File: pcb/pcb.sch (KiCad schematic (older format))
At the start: 116 parts, among them J1 USB_C_Receptacle_USB2.0, SW1 SW_Push, SW10 SW_Push, SW11 SW_Push, SW12 SW_Push, SW13 SW_Push, SW14 SW_Push, SW15 SW_Push, SW16 SW_Push, SW17 SW_Push, SW18 SW_Push, SW19 SW_Push, SW2 SW_Push, SW20 SW_Push, SW21 SW_Push, SW22 SW_Push, SW23 SW_Push, SW24 SW_Push, SW25 SW_Push, SW26 SW_Push, SW27 SW_Push, SW28 SW_Push, SW29 SW_Push, SW3 SW_Push, SW30 SW_Push, SW31 SW_Push, SW32 SW_Push, SW33 SW_Push, SW34 SW_Push, SW35 SW_Push, SW36 SW_Push, SW37 SW_Push, SW38 SW_Push, SW39 SW_Push, SW4 SW_Push, SW40 SW_Push, SW41 SW_Push, SW42 SW_Push, SW43 SW_Push, SW44 SW_Push, SW45 SW_Push, SW46 SW_Push, SW47 SW_Push, SW48 SW_Push, SW49 SW_Push, SW5 SW_Push, SW6 SW_Push, SW7 SW_Push, SW8 SW_Push, SW9 SW_Push, U1 ATmega32U4-AU, Y1 16MHz

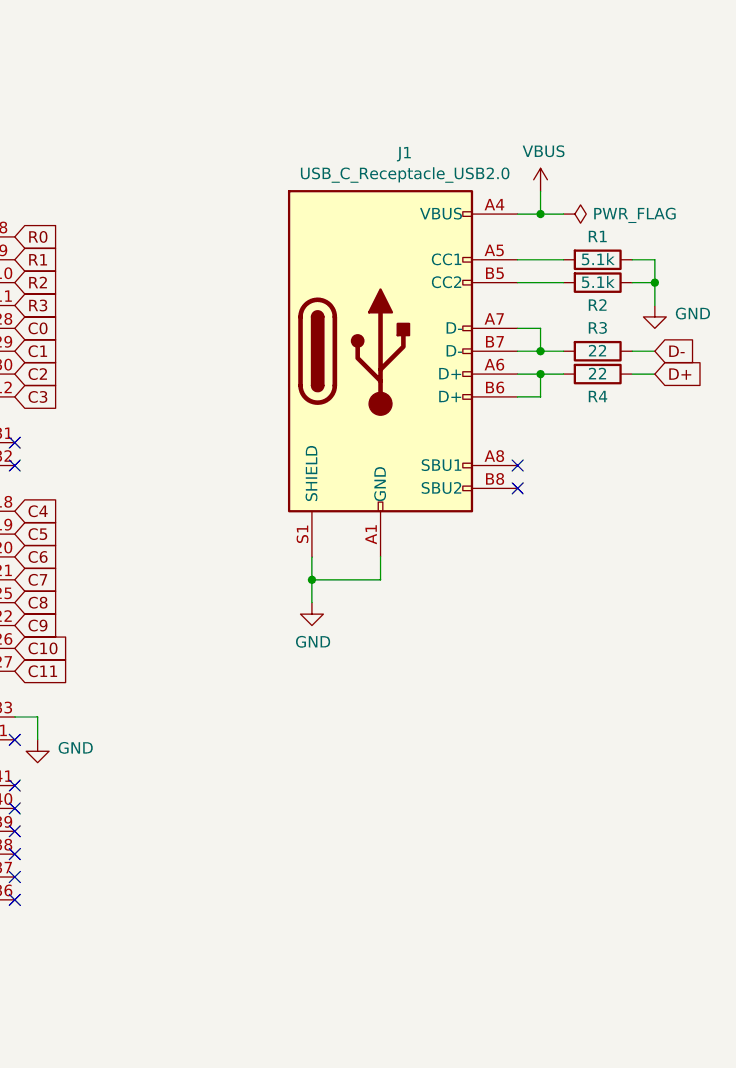
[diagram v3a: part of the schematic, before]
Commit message: update USB-C pins
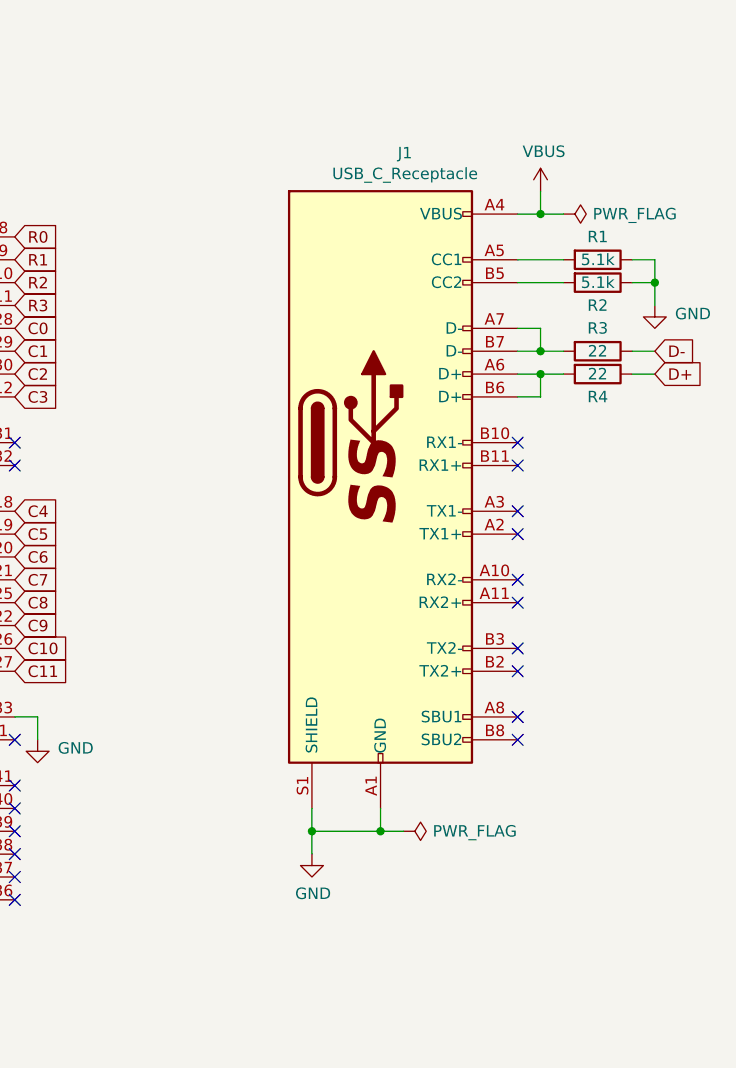
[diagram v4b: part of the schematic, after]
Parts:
- removed J1: USB_C_Receptacle_USB2.0, digikey-footprints:USB-C_Female_CX70M-24P1, symbol Connector:USB_C_Receptacle_USB2.0
- added J1: USB_C_Receptacle, digikey-footprints:USB-C_Female_CX70M-24P1, symbol Connector:USB_C_Receptacle
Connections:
- net GND: now also J1.A1 (GND), J1.A12 (GND), J1.B1 (GND), J1.B12 (GND), J1.S1 (SHIELD)
- net VBUS: now also J1.A4 (VBUS), J1.A9 (VBUS), J1.B4 (VBUS), J1.B9 (VBUS)
- net at R1.2: now also J1.A5 (CC1)
- net at R4.2: now also J1.A6 (D+), J1.B6 (D+)
- net at R3.2: now also J1.A7 (D-), J1.B7 (D-)
- net at R2.2: now also J1.B5 (CC2)
- no-connect marks 11 -> 19
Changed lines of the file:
@@
 	6350 5700 6350 5800
-$Comp
-L Connector:USB_C_Receptacle_USB2.0 J1
-U 1 1 5D13142D
-P 7850 4100
-F 0 "J1" H 7957 4967 50  0000 C CNN
-F 1 "USB_C_Receptacle_USB2.0" H 7957 4876 50  0000 C CNN
-F 2 "digikey-footprints:USB-C_Female_CX70M-24P1" H 8000 4100 50  0001 C CNN
-F 3 "https://www.usb.org/sites/default/files/documents/usb_type-c.zip" H 8000 4100 50  0001 C CNN
-	1    7850 4100
-	1    0    0    -1
-$EndComp
 $Comp
 L power:GND #PWR010
 U 1 1 5D1342DD
-P 7550 5200
-F 0 "#PWR010" H 7550 4950 50  0001 C CNN
-F 1 "GND" H 7555 5027 50  0000 C CNN
-F 2 "" H 7550 5200 50  0001 C CNN
-F 3 "" H 7550 5200 50  0001 C CNN
-	1    7550 5200
-	1    0    0    -1
-$EndComp
-Wire Wire Line
-	7550 5000 7550 5100
-Wire Wire Line
-	7550 5100 7850 5100
-Wire Wire Line
-	7850 5100 7850 5000
-Connection ~ 7550 5100
-Wire Wire Line
-	7550 5100 7550 5200
+P 7550 6300
+F 0 "#PWR010" H 7550 6050 50  0001 C CNN
+F 1 "GND" H 7555 6127 50  0000 C CNN
+F 2 "" H 7550 6300 50  0001 C CNN
+F 3 "" H 7550 6300 50  0001 C CNN
+	1    7550 6300
+	1    0    0    -1
+$EndComp
+Wire Wire Line
+	7550 6100 7550 6200
+Wire Wire Line
+	7550 6200 7850 6200
+Wire Wire Line
+	7850 6200 7850 6100
+Connection ~ 7550 6200
+Wire Wire Line
+	7550 6200 7550 6300
 NoConn ~ 8450 4600
-NoConn ~ 8450 4700
+NoConn ~ 8450 4500
 $Comp
 L power:VBUS #PWR02
@@
 	1    0    0    -1
 $EndComp
+$Comp
+L Connector:USB_C_Receptacle J1
+U 1 1 5D16305C
+P 7850 4500
+F 0 "J1" H 7957 5767 50  0000 C CNN
+F 1 "USB_C_Receptacle" H 7957 5676 50  0000 C CNN
+F 2 "digikey-footprints:USB-C_Female_CX70M-24P1" H 8000 4500 50  0001 C CNN
+F 3 "https://www.usb.org/sites/default/files/documents/usb_type-c.zip" H 8000 4500 50  0001 C CNN
+	1    7850 4500
+	1    0    0    -1
+$EndComp
+NoConn ~ 8450 4800
+NoConn ~ 8450 4900
+NoConn ~ 8450 5100
+NoConn ~ 8450 5200
+NoConn ~ 8450 5400
+NoConn ~ 8450 5500
+NoConn ~ 8450 5700
+NoConn ~ 8450 5800
+$Comp
+L power:PWR_FLAG #FLG02
+U 1 1 5D307145
+P 7950 6200
+F 0 "#FLG02" H 7950 6275 50  0001 C CNN
+F 1 "PWR_FLAG" V 7950 6328 50  0000 L CNN
+F 2 "" H 7950 6200 50  0001 C CNN
+F 3 "~" H 7950 6200 50  0001 C CNN
+	1    7950 6200
+	0    1    1    0
+$EndComp
+Wire Wire Line
+	7850 6200 7950 6200
+Connection ~ 7850 6200
 $EndSCHEMATC

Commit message: add PCB & gerber
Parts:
- removed C3: 0.1u, Capacitor_SMD:C_1206_3216Metric_Pad1.42x1.75mm_HandSolder, symbol Device:C
- removed R6, R7: 22, Resistor_SMD:R_1206_3216Metric_Pad1.42x1.75mm_HandSolder, symbol Device:R
- removed SW49: SW_Push, Button_Switch_THT:SW_PUSH_6mm_H5mm, symbol Switch:SW_Push
- added H1, H2, H3, H4, H5, H6, H7, H8: MountingHole, MountingHole:MountingHole_3.5mm, symbol Mechanical:MountingHole
- added JP1: SolderJumper_2_Open, Jumper:SolderJumper-2_P1.3mm_Open_Pad1.0x1.5mm, symbol Jumper:SolderJumper_2_Open
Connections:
- net VBUS is gone; now on net VCC: J1.A4 (VBUS), J1.A9 (VBUS), J1.B4 (VBUS), J1.B9 (VBUS), U1.7 (VBUS)
- net C0: now also U1.22 (PD5); no longer U1.28 (PB4)
- net C1: now also U1.21 (PD3); no longer U1.29 (PB5)
- net C11: now also U1.25 (PD4); no longer U1.27 (PD7)
- net C2: now also U1.20 (PD2); no longer U1.30 (PB6)
- net C3: now also U1.19 (PD1); no longer U1.12 (PB7)
- net C5: now also U1.12 (PB7); no longer U1.19 (PD1)
- net C6: now also U1.30 (PB6); no longer U1.20 (PD2)
- net C7: now also U1.29 (PB5); no longer U1.21 (PD3)
- net C8: now also U1.28 (PB4); no longer U1.25 (PD4)
- net C9: now also U1.27 (PD7); no longer U1.22 (PD5)
- net D+: now also U1.4 (D+)
- net D-: now also U1.3 (D-)
- net GND: now also JP1.2 (B)
- net RESET: now also JP1.1 (A)
- no-connect marks 19 -> 20
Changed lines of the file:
@@
 	1    0    0    -1
 $EndComp
-$Comp
-L Device:R R6
-U 1 1 5D0E382B
-P 4850 4600
-F 0 "R6" V 4750 4600 50  0000 C CNN
-F 1 "22" V 4850 4600 50  0000 C CNN
-F 2 "Resistor_SMD:R_1206_3216Metric_Pad1.42x1.75mm_HandSolder" H 4850 4600 50  0001 C CNN
-F 3 "~" H 4850 4600 50  0001 C CNN
-	1    4850 4600
-	0    1    1    0
-$EndComp
-Wire Wire Line
-	5000 4600 5050 4600
-Wire Wire Line
-	5000 4700 5050 4700
-Text GLabel 4650 4600 0    50   Input ~ 0
+Wire Wire Line
+	4950 4600 5050 4600
+Wire Wire Line
+	4950 4700 5050 4700
+Text GLabel 4950 4600 0    50   Input ~ 0
 D+
-Text GLabel 4650 4700 0    50   Input ~ 0
+Text GLabel 4950 4700 0    50   Input ~ 0
 D-
-Wire Wire Line
-	4650 4600 4700 4600
-Wire Wire Line
-	4650 4700 4700 4700
-$Comp
-L Device:R R7
-U 1 1 5D0E023D
-P 4850 4700
-F 0 "R7" V 4950 4700 50  0000 C CNN
-F 1 "22" V 4850 4700 50  0000 C CNN
-F 2 "Resistor_SMD:R_1206_3216Metric_Pad1.42x1.75mm_HandSolder" H 4850 4700 50  0001 C CNN
-F 3 "~" H 4850 4700 50  0001 C CNN
-	1    4850 4700
-	0    1    1    0
-$EndComp
 Wire Wire Line
 	2800 2400 2900 2400
@@
 	1    0    0    -1
 $EndComp
-Wire Wire Line
-	4400 4200 5050 4200
-Wire Wire Line
-	5050 4400 4600 4400
-Wire Wire Line
-	4600 4400 4600 4100
-$Comp
-L power:VBUS #PWR06
-U 1 1 5DD88E79
-P 4600 4100
-F 0 "#PWR06" H 4600 3950 50  0001 C CNN
-F 1 "VBUS" H 4543 4137 50  0000 R CNN
-F 2 "" H 4600 4100 50  0001 C CNN
-F 3 "" H 4600 4100 50  0001 C CNN
-	1    4600 4100
-	1    0    0    -1
-$EndComp
-$Comp
-L power:GND #PWR08
-U 1 1 5DD48EDC
-P 4400 4700
-F 0 "#PWR08" H 4400 4450 50  0001 C CNN
-F 1 "GND" H 4322 4663 50  0000 R CNN
-F 2 "" H 4400 4700 50  0001 C CNN
-F 3 "" H 4400 4700 50  0001 C CNN
-	1    4400 4700
-	1    0    0    -1
-$EndComp
-$Comp
-L Device:C C3
-U 1 1 5DD8B658
-P 4400 4450
-F 0 "C3" H 4285 4496 50  0000 R CNN
-F 1 "0.1u" H 4285 4405 50  0000 R CNN
-F 2 "Capacitor_SMD:C_1206_3216Metric_Pad1.42x1.75mm_HandSolder" H 4438 4300 50  0001 C CNN
-F 3 "~" H 4400 4450 50  0001 C CNN
-	1    4400 4450
-	1    0    0    -1
-$EndComp
-Wire Wire Line
-	4400 4300 4400 4200
-Wire Wire Line
-	4400 4700 4400 4600
 $Comp
 L Device:C C4
@@
 Text GLabel 6250 3900 2    50   Input ~ 0
 R3
-Text GLabel 6250 4000 2    50   Input ~ 0
+Text GLabel 6250 5300 2    50   Input ~ 0
 C0
-Text GLabel 6250 4100 2    50   Input ~ 0
+Text GLabel 6250 5100 2    50   Input ~ 0
 C1
-Text GLabel 6250 4200 2    50   Input ~ 0
+Text GLabel 6250 5000 2    50   Input ~ 0
 C2
-Text GLabel 6250 4300 2    50   Input ~ 0
+Text GLabel 6250 4900 2    50   Input ~ 0
 C3
 Text GLabel 6250 4800 2    50   Input ~ 0
 C4
-Text GLabel 6250 4900 2    50   Input ~ 0
+Text GLabel 6250 4300 2    50   Input ~ 0
 C5
-Text GLabel 6250 5000 2    50   Input ~ 0
+Text GLabel 6250 4200 2    50   Input ~ 0
 C6
-Text GLabel 6250 5100 2    50   Input ~ 0
+Text GLabel 6250 4100 2    50   Input ~ 0
 C7
-Text GLabel 6250 5200 2    50   Input ~ 0
+Text GLabel 6250 4000 2    50   Input ~ 0
 C8
-Text GLabel 6250 5300 2    50   Input ~ 0
+Text GLabel 6250 5500 2    50   Input ~ 0
 C9
 Text GLabel 6250 5400 2    50   Input ~ 0
 C10
-Text GLabel 6250 5500 2    50   Input ~ 0
+Text GLabel 6250 5200 2    50   Input ~ 0
 C11
 NoConn ~ 6250 4500
@@
 NoConn ~ 8450 4600
 NoConn ~ 8450 4500
-$Comp
-L power:VBUS #PWR02
-U 1 1 5D10FDDC
-P 8550 3400
-F 0 "#PWR02" H 8550 3250 50  0001 C CNN
-F 1 "VBUS" H 8565 3573 50  0000 C CNN
-F 2 "" H 8550 3400 50  0001 C CNN
-F 3 "" H 8550 3400 50  0001 C CNN
-	1    8550 3400
-	1    0    0    -1
-$EndComp
 Wire Wire Line
 	8450 3500 8550 3500
 Wire Wire Line
 	8550 3500 8550 3400
-Wire Wire Line
-	8650 3500 8550 3500
-Connection ~ 8550 3500
-$Comp
-L power:PWR_FLAG #FLG01
-U 1 1 5D148DCF
-P 8650 3500
-F 0 "#FLG01" H 8650 3575 50  0001 C CNN
-F 1 "PWR_FLAG" V 8650 3628 50  0000 L CNN
-F 2 "" H 8650 3500 50  0001 C CNN
-F 3 "~" H 8650 3500 50  0001 C CNN
-	1    8650 3500
-	0    1    1    0
-$EndComp
 $Comp
 L Device:R R1
@@
 	1    0    0    -1
 $EndComp
-$Comp
-L Switch:SW_Push SW49
-U 1 1 5D439BB1
-P 3050 4700
-F 0 "SW49" H 3150 4800 50  0000 C CNN
-F 1 "SW_Push" H 3050 4650 50  0000 C CNN
-F 2 "Button_Switch_THT:SW_PUSH_6mm_H5mm" H 3050 4900 50  0001 C CNN
-F 3 "~" H 3050 4900 50  0001 C CNN
-	1    3050 4700
-	1    0    0    -1
-$EndComp
 Wire Wire Line
 	2750 4500 2750 4700
@@
 	2750 4500 2850 4500
 Wire Wire Line
-	3250 4700 3350 4700
-Wire Wire Line
-	3350 4700 3350 4800
+	3150 4700 3250 4700
+Wire Wire Line
+	3250 4700 3250 4800
 $Comp
 L power:GND #PWR09
 U 1 1 5D47CC0F
-P 3350 4800
-F 0 "#PWR09" H 3350 4550 50  0001 C CNN
-F 1 "GND" H 3355 4627 50  0000 C CNN
-F 2 "" H 3350 4800 50  0001 C CNN
-F 3 "" H 3350 4800 50  0001 C CNN
-	1    3350 4800
+P 3250 4800
+F 0 "#PWR09" H 3250 4550 50  0001 C CNN
+F 1 "GND" H 3255 4627 50  0000 C CNN
+F 2 "" H 3250 4800 50  0001 C CNN
+F 3 "" H 3250 4800 50  0001 C CNN
+	1    3250 4800
 	1    0    0    -1
 $EndComp
@@
 NoConn ~ 8450 5800
 $Comp
-L power:PWR_FLAG #FLG02
-U 1 1 5D307145
+L power:VCC #PWR02
+U 1 1 5D441478
+P 8550 3400
+F 0 "#PWR02" H 8550 3250 50  0001 C CNN
+F 1 "VCC" H 8567 3573 50  0000 C CNN
+F 2 "" H 8550 3400 50  0001 C CNN
+F 3 "" H 8550 3400 50  0001 C CNN
+	1    8550 3400
+	1    0    0    -1
+$EndComp
+$Comp
+L power:VCC #PWR06
+U 1 1 5D467454
+P 4950 4300
+F 0 "#PWR06" H 4950 4150 50  0001 C CNN
+F 1 "VCC" H 4897 4337 50  0000 R CNN
+F 2 "" H 4950 4300 50  0001 C CNN
+F 3 "" H 4950 4300 50  0001 C CNN
+	1    4950 4300
+	1    0    0    -1
+$EndComp
+NoConn ~ 5050 4200
+Wire Wire Line
+	4950 4300 4950 4400
+Wire Wire Line
+	4950 4400 5050 4400
+$Comp
+L power:PWR_FLAG #FLG0101
+U 1 1 5D468AD3
+P 8650 3500
+F 0 "#FLG0101" H 8650 3575 50  0001 C CNN
+F 1 "PWR_FLAG" V 8650 3628 50  0000 L CNN
+F 2 "" H 8650 3500 50  0001 C CNN
+F 3 "~" H 8650 3500 50  0001 C CNN
+	1    8650 3500
+	0    1    1    0
+$EndComp
+Connection ~ 8550 3500
+$Comp
+L power:PWR_FLAG #FLG0102
+U 1 1 5D469CC2
 P 7950 6200
-F 0 "#FLG02" H 7950 6275 50  0001 C CNN
-F 1 "PWR_FLAG" V 7950 6328 50  0000 L CNN
+F 0 "#FLG0102" H 7950 6275 50  0001 C CNN
+F 1 "PWR_FLAG" V 7950 6327 50  0000 L CNN
 F 2 "" H 7950 6200 50  0001 C CNN
 F 3 "~" H 7950 6200 50  0001 C CNN
@@
 $EndComp
 Wire Wire Line
-	7850 6200 7950 6200
+	8650 3500 8550 3500
+Wire Wire Line
+	7950 6200 7850 6200
 Connection ~ 7850 6200
+$Comp
+L Jumper:SolderJumper_2_Open JP1
+U 1 1 5D25E77F
+P 3000 4700
+F 0 "JP1" H 3000 4600 50  0000 C CNN
+F 1 "SolderJumper_2_Open" H 3000 4814 50  0000 C CNN
+F 2 "Jumper:SolderJumper-2_P1.3mm_Open_Pad1.0x1.5mm" H 3000 4700 50  0001 C CNN
+F 3 "~" H 3000 4700 50  0001 C CNN
+	1    3000 4700
+	1    0    0    -1
+$EndComp
+$Comp
+L Mechanical:MountingHole H1
+U 1 1 5D31BC99
+P 2950 600
+F 0 "H1" H 3050 646 50  0000 L CNN
+F 1 "MountingHole" H 3050 555 50  0000 L CNN
+F 2 "MountingHole:MountingHole_3.5mm" H 2950 600 50  0001 C CNN
+F 3 "~" H 2950 600 50  0001 C CNN
+	1    2950 600
+	1    0    0    -1
+$EndComp
+$Comp
+L Mechanical:MountingHole H5
+U 1 1 5D31E66D
+P 2950 800
+F 0 "H5" H 3050 846 50  0000 L CNN
+F 1 "MountingHole" H 3050 755 50  0000 L CNN
+F 2 "MountingHole:MountingHole_3.5mm" H 2950 800 50  0001 C CNN
+F 3 "~" H 2950 800 50  0001 C CNN
+	1    2950 800
+	1    0    0    -1
+$EndComp
+$Comp
+L Mechanical:MountingHole H4
+U 1 1 5D31F448
+P 8400 600
+F 0 "H4" H 8500 646 50  0000 L CNN
+F 1 "MountingHole" H 8500 555 50  0000 L CNN
+F 2 "MountingHole:MountingHole_3.5mm" H 8400 600 50  0001 C CNN
+F 3 "~" H 8400 600 50  0001 C CNN
+	1    8400 600
+	1    0    0    -1
+$EndComp
+$Comp
+L Mechanical:MountingHole H8
+U 1 1 5D31F44E
+P 8400 800
+F 0 "H8" H 8500 846 50  0000 L CNN
+F 1 "MountingHole" H 8500 755 50  0000 L CNN
+F 2 "MountingHole:MountingHole_3.5mm" H 8400 800 50  0001 C CNN
+F 3 "~" H 8400 800 50  0001 C CNN
+	1    8400 800
+	1    0    0    -1
+$EndComp
+$Comp
+L Mechanical:MountingHole H2
+U 1 1 5D3FB5DB
+P 4600 600
+F 0 "H2" H 4700 646 50  0000 L CNN
+F 1 "MountingHole" H 4700 555 50  0000 L CNN
+F 2 "MountingHole:MountingHole_3.5mm" H 4600 600 50  0001 C CNN
+F 3 "~" H 4600 600 50  0001 C CNN
+	1    4600 600
+	1    0    0    -1
+$EndComp
+$Comp
+L Mechanical:MountingHole H6
+U 1 1 5D3FB5E1
+P 4600 800
+F 0 "H6" H 4700 846 50  0000 L CNN
+F 1 "MountingHole" H 4700 755 50  0000 L CNN
+F 2 "MountingHole:MountingHole_3.5mm" H 4600 800 50  0001 C CNN
+F 3 "~" H 4600 800 50  0001 C CNN
+	1    4600 800
+	1    0    0    -1
+$EndComp
+$Comp
+L Mechanical:MountingHole H3
+U 1 1 5D41FF38
+P 6750 600
+F 0 "H3" H 6850 646 50  0000 L CNN
+F 1 "MountingHole" H 6850 555 50  0000 L CNN
+F 2 "MountingHole:MountingHole_3.5mm" H 6750 600 50  0001 C CNN
+F 3 "~" H 6750 600 50  0001 C CNN
+	1    6750 600
+	1    0    0    -1
+$EndComp
+$Comp
+L Mechanical:MountingHole H7
+U 1 1 5D41FF3E
+P 6750 800
+F 0 "H7" H 6850 846 50  0000 L CNN
+F 1 "MountingHole" H 6850 755 50  0000 L CNN
+F 2 "MountingHole:MountingHole_3.5mm" H 6750 800 50  0001 C CNN
+F 3 "~" H 6750 800 50  0001 C CNN
+	1    6750 800
+	1    0    0    -1
+$EndComp
 $EndSCHEMATC
